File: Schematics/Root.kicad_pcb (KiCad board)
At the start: 2 copper layers, 100 x 100 mm, 138 parts, among them CON301 USB-MICRO-B, IC301 ATXMEGA256A3BU-A, J301 AVR_JTAG_Header, U1 LM324, U1001 PCA9685, U1101 PCA9685, U1201 PCA9685, U1301 PCA9685, U1401 PCA9685, U1501 PCA9685, U1601 PCA9685, U501 PCA9685, U601 PCA9685, U701 PCA9685, U801 PCA9685, U901 PCA9685

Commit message: LEDs are placed!
Worked out how to script KiCAD to do it too. Winner winner, time for a chicken dinner
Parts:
- removed C1001, C1101, C1201, C1301, C1401, C1501, C1601, C301, C302, C303, C304, C501, C601, C701, C801, C901: C, Capacitors_SMD:C_0603
- removed C201, C305, C311: 1u, Capacitors_SMD:C_0603
- removed C306, C307, C308, C309, C310: 100n, Capacitors_SMD:C_0603
- removed CON301: USB-MICRO-B, Connect:USB_Micro-B
- removed D1001, D1002, D1003, D1004, D1005, D1101, D1102, D1103, D1104, D1105, D1201, D1202, D1203, D1204, D1205, D1301, D1302, D1303, D1304, D1305, D1401, D1402, D1403, D1404, D1405, D1501, D1502, D1503, D1504, D1505, D1601, D1602, D1603, D1604, D1605, D501, D502, D503, D504, D505, D601, D602, D603, D604, D605, D701, D702, D703, D704, D705, D801, D802, D803, D804, D805, D901, D902, D903, D904, D905: LED_RGB, rgb:rgbled1
- removed IC301: ATXMEGA256A3BU-A, SMD_Packages:TQFP-64
- removed J301: AVR_JTAG_Header, Socket_Strips:Socket_Strip_Straight_2x05
- removed R1001, R1101, R1201, R1301, R1401, R1501, R1601, R501, R601, R701, R801, R901: 10k, Resistors_SMD:R_0603
- removed R301: 100R, Resistors_SMD:R_0603
- removed R302: 50R, Resistors_SMD:R_0603
- removed R303, R304: 47k, Resistors_SMD:R_0603
- removed U1001, U1101, U1201, U1301, U1401, U1501, U1601, U501, U601, U701, U801, U901: PCA9685, Housings_DFN_QFN:QFN-28-1EP_6x6mm_Pitch0.65mm
- added C10: C, Capacitors_SMD:C_0603, F.Cu at (248.8, 50.9)
- added C11: C, Capacitors_SMD:C_0603, F.Cu at (238.9, 59.1)
- added C12: C, Capacitors_SMD:C_0603, F.Cu at (257.7, 37.9)
- added C13: C, Capacitors_SMD:C_0603, F.Cu at (243.0, 52.6)
- added C14: 1u, Capacitors_SMD:C_0603, F.Cu at (234.0, 52.6)
- added C15: 100n, Capacitors_SMD:C_0603, F.Cu at (249.2, 44.4)
- added C16: 100n, Capacitors_SMD:C_0603, F.Cu at (238.5, 52.6)
- added C17: 100n, Capacitors_SMD:C_0603, F.Cu at (253.2, 37.9)
- added C18: 100n, Capacitors_SMD:C_0603, F.Cu at (234.4, 59.1)
- added C19: 100n, Capacitors_SMD:C_0603, F.Cu at (253.2, 50.9)
- added C20: 1u, Capacitors_SMD:C_0603, F.Cu at (248.8, 37.9)
- added C21: C, Capacitors_SMD:C_0603, F.Cu at (287.6, 49.6)
- added C22: C, Capacitors_SMD:C_0603, F.Cu at (238.4, 106.2)
- added C23: C, Capacitors_SMD:C_0603, F.Cu at (281.0, 80.9)
- added C24: C, Capacitors_SMD:C_0603, F.Cu at (333.5, 49.6)
- added C25: C, Capacitors_SMD:C_0603, F.Cu at (364.1, 99.4)
- added C26: C, Capacitors_SMD:C_0603, F.Cu at (280.2, 106.2)
- added C27: C, Capacitors_SMD:C_0603, F.Cu at (322.3, 74.5)
- added C28: C, Capacitors_SMD:C_0603, F.Cu at (363.0, 124.2)
- added C29: C, Capacitors_SMD:C_0603, F.Cu at (371.2, 49.6)
- added C30: C, Capacitors_SMD:C_0603, F.Cu at (318.7, 99.4)
- added C31: C, Capacitors_SMD:C_0603, F.Cu at (360.5, 74.5)
- added C32: C, Capacitors_SMD:C_0603, F.Cu at (322.0, 124.2)
- added C9: 100n, Capacitors_SMD:C_0603, F.Cu at (225.4, 82.1)
- added CON1: USB-MICRO-B, Connect:USB_Micro-B, F.Cu at (243.6, 40.5)
- added IC1: ATXMEGA256A3BU-A, SMD_Packages:TQFP-64, F.Cu at (105.5, 85.2)
- added J1: AVR_JTAG_Header, Socket_Strips:Socket_Strip_Straight_2x05, F.Cu at (225.0, 54.2)
- added LED1: LED_RGB, rgb:rgbled1, F.Cu at (100.6, 38.5)
- added LED10: LED_RGB, rgb:rgbled1, F.Cu at (64.8, 61.7)
- added LED11: LED_RGB, rgb:rgbled1, F.Cu at (62.6, 66.1)
- added LED12: LED_RGB, rgb:rgbled1, F.Cu at (60.8, 70.7)
- added LED13: LED_RGB, rgb:rgbled1, F.Cu at (59.5, 75.4)
- added LED14: LED_RGB, rgb:rgbled1, F.Cu at (58.8, 80.3)
- added LED15: LED_RGB, rgb:rgbled1, F.Cu at (58.5, 85.2)
- added LED16: LED_RGB, rgb:rgbled1, F.Cu at (58.8, 90.1)
- added LED17: LED_RGB, rgb:rgbled1, F.Cu at (59.5, 95.0)
- added LED18: LED_RGB, rgb:rgbled1, F.Cu at (60.8, 99.7)
- added LED19: LED_RGB, rgb:rgbled1, F.Cu at (62.6, 104.3)
- added LED2: LED_RGB, rgb:rgbled1, F.Cu at (95.7, 39.2)
- added LED20: LED_RGB, rgb:rgbled1, F.Cu at (64.8, 108.7)
- added LED21: LED_RGB, rgb:rgbled1, F.Cu at (67.5, 112.8)
- added LED22: LED_RGB, rgb:rgbled1, F.Cu at (70.6, 116.6)
- added LED23: LED_RGB, rgb:rgbled1, F.Cu at (74.1, 120.1)
- added LED24: LED_RGB, rgb:rgbled1, F.Cu at (77.9, 123.2)
- added LED25: LED_RGB, rgb:rgbled1, F.Cu at (82.0, 125.9)
- added LED26: LED_RGB, rgb:rgbled1, F.Cu at (86.4, 128.1)
- added LED27: LED_RGB, rgb:rgbled1, F.Cu at (91.0, 129.9)
- added LED28: LED_RGB, rgb:rgbled1, F.Cu at (95.7, 131.2)
- added LED29: LED_RGB, rgb:rgbled1, F.Cu at (100.6, 131.9)
- added LED3: LED_RGB, rgb:rgbled1, F.Cu at (91.0, 40.5)
- added LED30: LED_RGB, rgb:rgbled1, F.Cu at (105.5, 132.2)
- added LED31: LED_RGB, rgb:rgbled1, F.Cu at (110.4, 131.9)
- added LED32: LED_RGB, rgb:rgbled1, F.Cu at (115.3, 131.2)
- added LED33: LED_RGB, rgb:rgbled1, F.Cu at (120.0, 129.9)
- added LED34: LED_RGB, rgb:rgbled1, F.Cu at (124.6, 128.1)
- added LED35: LED_RGB, rgb:rgbled1, F.Cu at (129.0, 125.9)
- added LED36: LED_RGB, rgb:rgbled1, F.Cu at (133.1, 123.2)
- added LED37: LED_RGB, rgb:rgbled1, F.Cu at (136.9, 120.1)
- added LED38: LED_RGB, rgb:rgbled1, F.Cu at (140.4, 116.6)
- added LED39: LED_RGB, rgb:rgbled1, F.Cu at (143.5, 112.8)
- added LED4: LED_RGB, rgb:rgbled1, F.Cu at (86.4, 42.3)
- added LED40: LED_RGB, rgb:rgbled1, F.Cu at (146.2, 108.7)
- added LED41: LED_RGB, rgb:rgbled1, F.Cu at (148.4, 104.3)
- added LED42: LED_RGB, rgb:rgbled1, F.Cu at (150.2, 99.7)
- added LED43: LED_RGB, rgb:rgbled1, F.Cu at (151.5, 95.0)
- added LED44: LED_RGB, rgb:rgbled1, F.Cu at (152.2, 90.1)
- added LED45: LED_RGB, rgb:rgbled1, F.Cu at (152.5, 85.2)
- added LED46: LED_RGB, rgb:rgbled1, F.Cu at (152.2, 80.3)
- added LED47: LED_RGB, rgb:rgbled1, F.Cu at (151.5, 75.4)
- added LED48: LED_RGB, rgb:rgbled1, F.Cu at (150.2, 70.7)
- added LED49: LED_RGB, rgb:rgbled1, F.Cu at (148.4, 66.1)
- added LED5: LED_RGB, rgb:rgbled1, F.Cu at (82.0, 44.5)
- added LED50: LED_RGB, rgb:rgbled1, F.Cu at (146.2, 61.7)
- added LED51: LED_RGB, rgb:rgbled1, F.Cu at (143.5, 57.6)
- added LED52: LED_RGB, rgb:rgbled1, F.Cu at (140.4, 53.8)
- added LED53: LED_RGB, rgb:rgbled1, F.Cu at (136.9, 50.3)
- added LED54: LED_RGB, rgb:rgbled1, F.Cu at (133.1, 47.2)
- added LED55: LED_RGB, rgb:rgbled1, F.Cu at (129.0, 44.5)
- added LED56: LED_RGB, rgb:rgbled1, F.Cu at (124.6, 42.3)
- added LED57: LED_RGB, rgb:rgbled1, F.Cu at (120.0, 40.5)
- added LED58: LED_RGB, rgb:rgbled1, F.Cu at (115.3, 39.2)
- added LED59: LED_RGB, rgb:rgbled1, F.Cu at (110.4, 38.5)
- added LED6: LED_RGB, rgb:rgbled1, F.Cu at (77.9, 47.2)
- added LED60: LED_RGB, rgb:rgbled1, F.Cu at (105.5, 38.2)
- added LED7: LED_RGB, rgb:rgbled1, F.Cu at (74.1, 50.3)
- added LED8: LED_RGB, rgb:rgbled1, F.Cu at (70.6, 53.8)
- added LED9: LED_RGB, rgb:rgbled1, F.Cu at (67.5, 57.6)
- added R15: 100R, Resistors_SMD:R_0603, F.Cu at (254.2, 44.4)
- added R16: 50R, Resistors_SMD:R_0603, F.Cu at (258.7, 44.4)
- added R17: 47k, Resistors_SMD:R_0603, F.Cu at (261.8, 37.9)
- added R18: 47k, Resistors_SMD:R_0603, F.Cu at (243.0, 59.1)
- added R19: 10k, Resistors_SMD:R_0603, F.Cu at (291.7, 49.6)
- added R20: 10k, Resistors_SMD:R_0603, F.Cu at (234.4, 106.2)
- added R21: 10k, Resistors_SMD:R_0603, F.Cu at (276.9, 80.9)
- added R22: 10k, Resistors_SMD:R_0603, F.Cu at (329.4, 49.6)
- added R23: 10k, Resistors_SMD:R_0603, F.Cu at (360.1, 99.4)
- added R24: 10k, Resistors_SMD:R_0603, F.Cu at (276.2, 106.2)
- added R25: 10k, Resistors_SMD:R_0603, F.Cu at (318.3, 74.5)
- added R26: 10k, Resistors_SMD:R_0603, F.Cu at (358.9, 124.2)
- added R27: 10k, Resistors_SMD:R_0603, F.Cu at (375.3, 49.6)
- added R28: 10k, Resistors_SMD:R_0603, F.Cu at (322.8, 99.4)
- added R29: 10k, Resistors_SMD:R_0603, F.Cu at (364.6, 74.5)
- added R30: 10k, Resistors_SMD:R_0603, F.Cu at (318.0, 124.2)
- added U10: PCA9685, Housings_DFN_QFN:QFN-28-1EP_6x6mm_Pitch0.65mm, F.Cu at (345.8, 40.3)
- added U11: PCA9685, Housings_DFN_QFN:QFN-28-1EP_6x6mm_Pitch0.65mm, F.Cu at (335.1, 90.0)
- added U12: PCA9685, Housings_DFN_QFN:QFN-28-1EP_6x6mm_Pitch0.65mm, F.Cu at (334.4, 114.9)
- added U2: PCA9685, Housings_DFN_QFN:QFN-28-1EP_6x6mm_Pitch0.65mm, F.Cu at (334.7, 65.2)
- added U20: LM324, SMD_Packages:TSSOP-14, F.Cu at (221.0, 69.8)
- added U3: PCA9685, Housings_DFN_QFN:QFN-28-1EP_6x6mm_Pitch0.65mm, F.Cu at (304.0, 40.3)
- added U4: PCA9685, Housings_DFN_QFN:QFN-28-1EP_6x6mm_Pitch0.65mm, F.Cu at (293.3, 71.6)
- added U5: PCA9685, Housings_DFN_QFN:QFN-28-1EP_6x6mm_Pitch0.65mm, F.Cu at (387.6, 40.3)
- added U6: PCA9685, Housings_DFN_QFN:QFN-28-1EP_6x6mm_Pitch0.65mm, F.Cu at (376.9, 65.2)
- added U7: PCA9685, Housings_DFN_QFN:QFN-28-1EP_6x6mm_Pitch0.65mm, F.Cu at (292.6, 96.9)
- added U8: PCA9685, Housings_DFN_QFN:QFN-28-1EP_6x6mm_Pitch0.65mm, F.Cu at (374.5, 114.9)
- added U9: PCA9685, Housings_DFN_QFN:QFN-28-1EP_6x6mm_Pitch0.65mm, F.Cu at (250.8, 96.9)
- C7: value 100n -> 1u
- U1: value LM324 -> PCA9685; footprint SMD_Packages:TSSOP-14 -> Housings_DFN_QFN:QFN-28-1EP_6x6mm_Pitch0.65mm
- moved R4 134.1 mm to (252.1, 69.1)
- moved R7 133.4 mm to (247.8, 69.1), turned to 0 degrees
- moved R11 132.5 mm to (247.6, 82.0)
- moved R3 131.4 mm to (246.6, 75.6), turned to 0 degrees
- moved R2 128.6 mm to (250.5, 75.6), turned to 0 degrees
- moved R14 125.1 mm to (239.8, 69.1)
- moved R1 122.2 mm to (243.6, 82.1), turned to 0 degrees
- moved R10 121.1 mm to (243.8, 69.1), turned to 0 degrees
- moved R8 121.0 mm to (242.7, 75.6), turned to 0 degrees
- moved R9 119.1 mm to (238.8, 75.6), turned to 0 degrees
- moved R5 117.9 mm to (239.3, 82.1)
- moved C3 115.9 mm to (235.8, 69.1), turned to 0 degrees
- moved C8 115.7 mm to (230.4, 75.6), turned to 0 degrees
- moved R6 115.2 mm to (234.4, 82.1), turned to 0 degrees
- moved R12 113.1 mm to (234.9, 75.6), turned to 0 degrees
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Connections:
- C7 pad 1: Net-(C7-Pad1) -> GND
- C7 pad 2: Net-(C7-Pad2) -> VPP
- C8 pad 2: Net-(C7-Pad2) -> Net-(C8-Pad2)
- R10 pad 1: Net-(C7-Pad2) -> Net-(C8-Pad2)
- R11 pad 1: Net-(C8-Pad1) -> Net-(C9-Pad1)
- R11 pad 2: Net-(C7-Pad1) -> Net-(C8-Pad1)
- R14 pad 2: Net-(C8-Pad1) -> Net-(C9-Pad1)
- U1 pad 1: Net-(R7-Pad2) -> GND
- U1 pad 10: /Amp and Filter/V_com -> Net-(LED3-PadGC)
- U1 pad 12: /Amp and Filter/V_com -> Net-(LED3-PadBC)
- U1 pad 13: Net-(C7-Pad1) -> Net-(LED4-PadRC)
- U1 pad 14: Net-(C8-Pad1) -> Net-(LED4-PadGC)
- U1 pad 2: Net-(C2-Pad1) -> VPP
- U1 pad 3: /Amp and Filter/V_com -> Net-(LED1-PadRC)
- U1 pad 4: VPP -> Net-(LED1-PadGC)
- U1 pad 5: GND -> Net-(LED1-PadBC)
- U1 pad 6: Net-(R6-Pad1) -> Net-(LED2-PadRC)
- U1 pad 7: /Amp and Filter/AMP_OUT -> Net-(LED2-PadGC)
- U1 pad 8: Net-(C6-Pad1) -> Net-(LED2-PadBC)
- U1 pad 9: Net-(C5-Pad1) -> Net-(LED3-PadRC)

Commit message: Latest schematics and pcb.
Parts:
- added BT1: 3V, rgb:BU2032SM-HD-GTR-ND, F.Cu at (128.1, 85.1)
- added C1: C, Capacitors_SMD:C_1206, F.Cu at (92.8, 61.7)
- added JP1: JUMPER, SMD_Packages:SMD-0201_r, F.Cu at (99.1, 80.3)
- added R100: 100k, Resistors_SMD:R_0603, F.Cu at (97.7, 80.4)
- added X1: 12MHz, Crystals_Oscillators_SMD:crystal_FA238-TSX3225, F.Cu at (104.7, 76.6)
- added X2: 32.768KhZ, Crystals_Oscillators_SMD:crystal_FA238-TSX3225, F.Cu at (114.2, 84.1)
- CON1: footprint Connect:USB_Micro-B -> usb:USB_Micro-B; moved to B.Cu
- J1: footprint Socket_Strips:Socket_Strip_Straight_2x05 -> rgb:FTSH-105-01-L-DV-K-A-P
- R11: footprint Resistors_SMD:R_0402 -> Resistors_SMD:R_0603
- U20: footprint SMD_Packages:TSSOP-14 -> Housings_SOIC:SOIC-14_3.9x8.7mm_Pitch1.27mm
- moved U5 317.8 mm to (78.7, 114.9), turned to 318 degrees
- moved R27 298.9 mm to (83.1, 112.8)
- moved C29 296.5 mm to (81.1, 110.8)
- moved U6 285.9 mm to (97.2, 124.3), turned to 348 degrees
- moved C25 280.5 mm to (87.8, 51.0)
- moved R23 271.2 mm to (92.7, 54.0)
- moved C31 267.8 mm to (96.6, 119.8)
- moved R29 267.8 mm to (100.7, 119.8)
- moved U2 259.0 mm to (75.8, 58.4), turned to 228 degrees
- moved R25 242.3 mm to (76.2, 63.6)
- moved C27 241.3 mm to (81.6, 57.4)
- moved U3 240.4 mm to (66.4, 76.9), turned to 258 degrees
- moved U8 239.3 mm to (135.2, 112.0), turned to 48 degrees
- moved U12 231.0 mm to (113.8, 46.1), turned to 168 degrees
- moved C28 230.9 mm to (132.7, 107.2)
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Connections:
- IC1 pad 2: Net-(IC1-Pad2) -> (no net)
- IC1 pad 3: Net-(IC1-Pad3) -> (no net)
- IC1 pad 36: Net-(IC1-Pad36) -> (no net)
- IC1 pad 37: Net-(IC1-Pad37) -> (no net)
- IC1 pad 38: Net-(IC1-Pad38) -> (no net)
- IC1 pad 39: Net-(IC1-Pad39) -> (no net)
- IC1 pad 4: Net-(IC1-Pad4) -> (no net)
- IC1 pad 40: Net-(IC1-Pad40) -> (no net)
- IC1 pad 41: Net-(IC1-Pad41) -> (no net)
- IC1 pad 46: Net-(IC1-Pad46) -> (no net)
- IC1 pad 47: Net-(IC1-Pad47) -> (no net)
- IC1 pad 48: Net-(IC1-Pad48) -> (no net)
- IC1 pad 49: Net-(IC1-Pad49) -> (no net)
- IC1 pad 5: Net-(IC1-Pad5) -> /Microcontroller/RF_In
- IC1 pad 50: Net-(IC1-Pad50) -> (no net)
- IC1 pad 54: Net-(IC1-Pad54) -> (no net)
- IC1 pad 55: Net-(IC1-Pad55) -> (no net)
- IC1 pad 56: Net-(IC1-Pad56) -> (no net)
- IC1 pad 6: Net-(IC1-Pad6) -> (no net)
- IC1 pad 62: /Microcontroller/RF_In -> (no net)
- IC1 pad 63: Net-(IC1-Pad63) -> (no net)
- IC1 pad 64: Net-(IC1-Pad64) -> (no net)
- IC1 pad 7: Net-(IC1-Pad7) -> (no net)
- IC1 pad 8: Net-(IC1-Pad8) -> (no net)
- IC1 pad 9: Net-(IC1-Pad9) -> (no net)
- J1 pad 7: Net-(J1-Pad7) -> (no net)
- J1 pad 8: Net-(J1-Pad8) -> (no net)
- U1 pad 19: Net-(U1-Pad19) -> (no net)
- U10 pad 19: Net-(U10-Pad19) -> (no net)
- U11 pad 19: Net-(U11-Pad19) -> (no net)
- U12 pad 19: Net-(U12-Pad19) -> (no net)
- U2 pad 19: Net-(U2-Pad19) -> (no net)
- U3 pad 19: Net-(U3-Pad19) -> (no net)
- U4 pad 19: Net-(U4-Pad19) -> (no net)
- U5 pad 19: Net-(U5-Pad19) -> (no net)
- U6 pad 19: Net-(U6-Pad19) -> (no net)
- U7 pad 19: Net-(U7-Pad19) -> (no net)
- U8 pad 19: Net-(U8-Pad19) -> (no net)
- U9 pad 19: Net-(U9-Pad19) -> (no net)
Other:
- net class Clock removed
- net class Default: clearance 0.254 -> 0.15; trace_width 0.254 -> 0.15; via_dia 0.889 -> 0.3; via_drill 0.635 -> 0.25
- net class Power removed
- rule trace_clearance: 0.254 -> 0.15
- rule trace_min: 0.254 -> 0.15
- rule via_min_drill: 0.508 -> 0.25
- rule via_min_size: 0.889 -> 0.3

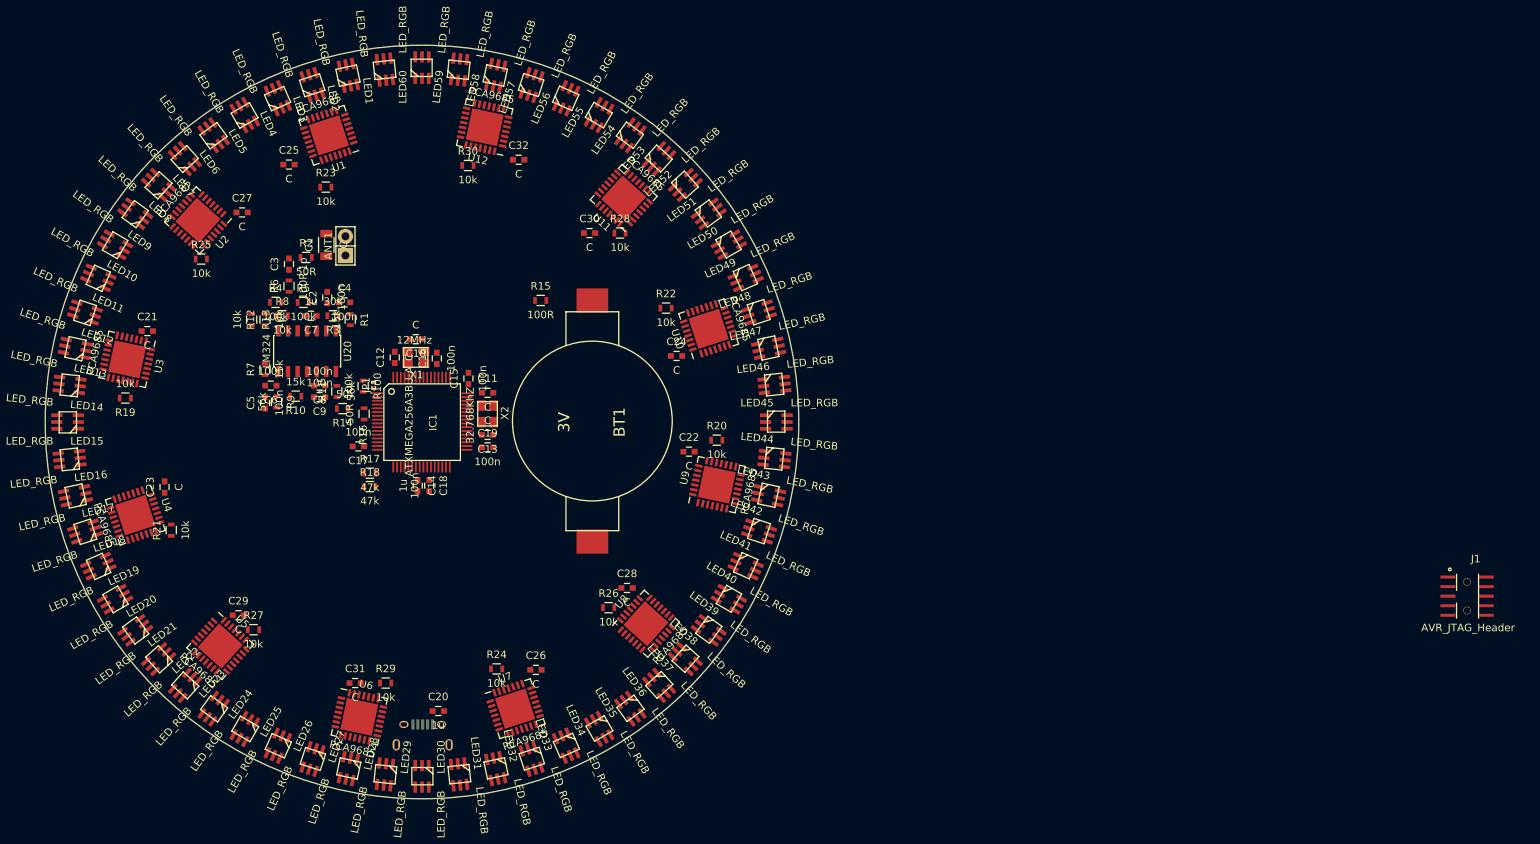
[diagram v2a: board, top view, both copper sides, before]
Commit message: Removed RF. Placed all LED drivers and passives and begun routing
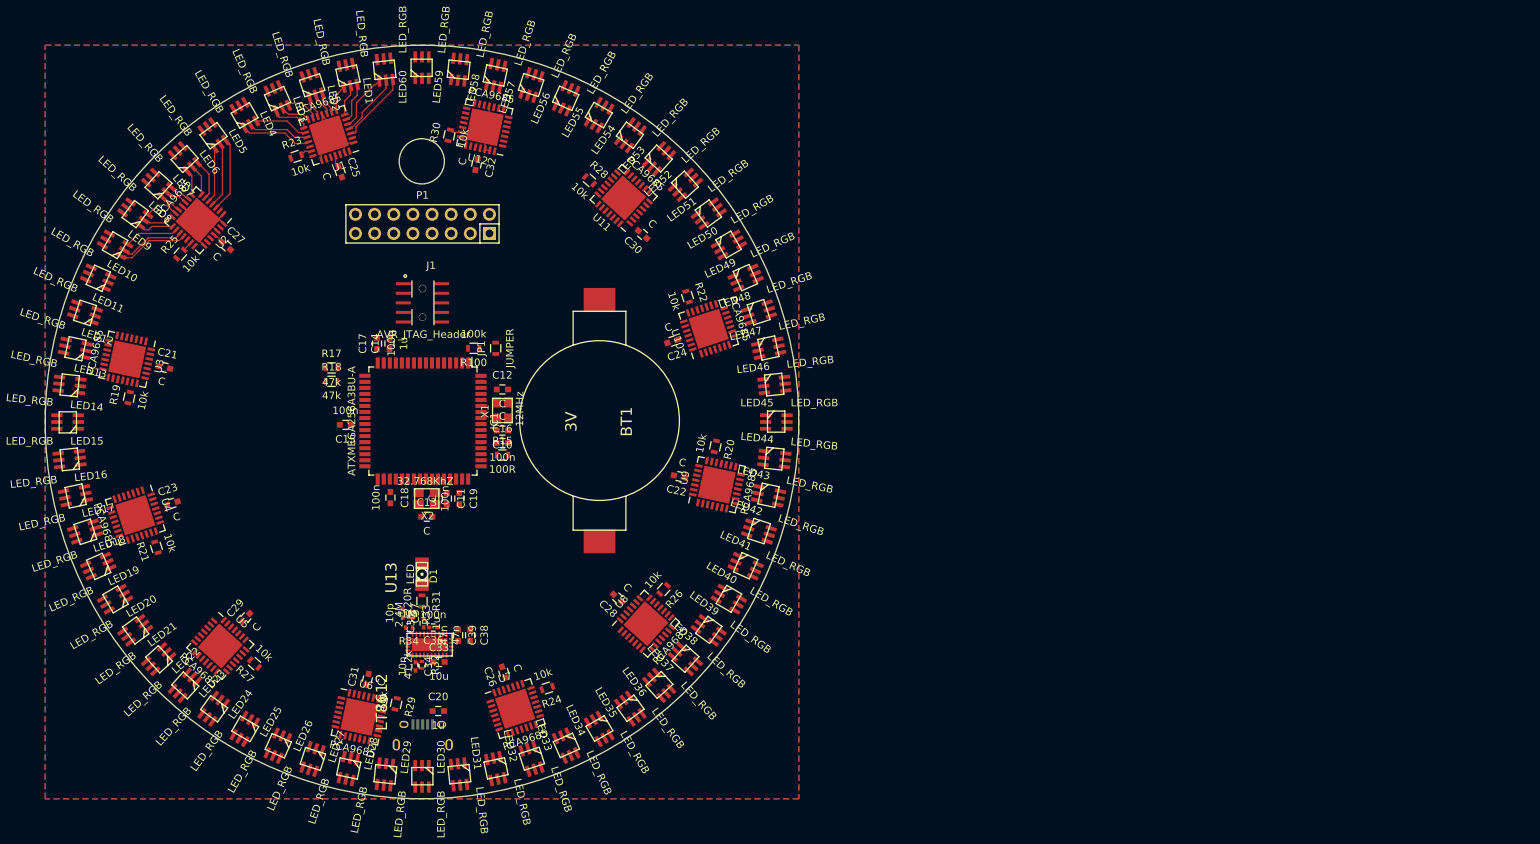
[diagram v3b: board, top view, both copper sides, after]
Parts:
- removed ANT1: ANT, Pin_Headers:Pin_Header_Straight_1x02
- removed C1: C, Capacitors_SMD:C_1206
- removed C2, C4, C5, C6, C8, C9: 100n, Capacitors_SMD:C_0603
- removed C3: 1p, Capacitors_SMD:C_0603
- removed C7: 1u, Capacitors_SMD:C_0603
- removed R1, R10, R7: 15k, Resistors_SMD:R_0603
- removed R11, R9: 56k, Resistors_SMD:R_0603
- removed R12, R13, R8: 10k, Resistors_SMD:R_0603
- removed R14: 50, Resistors_SMD:R_0603
- removed R16, R2: 50R, Resistors_SMD:R_0603
- removed R3: 30k, Resistors_SMD:R_0603
- removed R4, R5: 100k, Resistors_SMD:R_0603
- removed R6: 100R, Resistors_SMD:R_0603
- removed U20: LM324, Housings_SOIC:SOIC-14_3.9x8.7mm_Pitch1.27mm
- added C33: 10u, Capacitors_SMD:C_0603, F.Cu at (107.8, 117.0)
- added C34: 10n, Capacitors_SMD:C_0402, F.Cu at (104.6, 117.6)
- added C35: 1u, Capacitors_SMD:C_0402, F.Cu at (105.7, 111.9)
- added C36: 100n, Capacitors_SMD:C_0402, F.Cu at (107.0, 112.5)
- added C37: 10p, Capacitors_SMD:C_0402, F.Cu at (102.9, 110.6)
- added C38: 47n, Capacitors_SMD:C_0603, F.Cu at (111.9, 113.5)
- added C39: 47n, Capacitors_SMD:C_0603, F.Cu at (110.3, 113.5)
- added D1: LED, LEDs:LED-1206, F.Cu at (105.5, 105.4)
- added P1: CONN_02X08, Socket_Strips:Socket_Strip_Straight_2x08, F.Cu at (105.6, 58.9)
- added R31: 220R, Resistors_SMD:R_0603, F.Cu at (105.5, 108.9)
- added R32: 41.2k, Resistors_SMD:R_0402, F.Cu at (105.5, 117.4)
- added R33: 2.4M, Resistors_SMD:R_0402, F.Cu at (104.3, 110.8)
- added R34: 1M, Resistors_SMD:R_0402, F.Cu at (103.8, 112.5)
- added U13: LT8612, rgb:28QFN, F.Cu at (106.5, 114.8)
- IC1: footprint SMD_Packages:TQFP-64 -> Housings_QFP:TQFP-64_14x14mm_Pitch0.8mm
- JP1: footprint SMD_Packages:SMD-0201_r -> Resistors_SMD:R_0603
- moved J1 144.0 mm to (105.6, 69.4)
- moved R15 21.1 mm to (116.2, 89.6)
- moved C14 19.2 mm to (101.2, 74.8), turned to 90 degrees
- moved C15 17.4 mm to (95.3, 85.6), turned to 180 degrees
- moved JP1 16.9 mm to (115.3, 75.4)
- moved C10 16.7 mm to (116.2, 86.3)
- moved R100 15.5 mm to (112.4, 75.4), turned to 180 degrees
- moved C11 15.0 mm to (108.8, 95.4), turned to 270 degrees
- moved C12 14.9 mm to (116.2, 80.9), turned to 0 degrees
- moved R17 14.9 mm to (93.5, 78.0)
- moved R18 14.9 mm to (93.5, 79.8)
- moved C16 14.2 mm to (116.2, 88.0), turned to 0 degrees
- moved C17 13.9 mm to (99.5, 74.8), turned to 90 degrees
- moved X2 13.8 mm to (106.1, 95.4), turned to 180 degrees
- moved C13 13.5 mm to (106.1, 97.8), turned to 0 degrees
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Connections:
- net Net-(C20-Pad1) renamed /Power Supply/Vin
- IC1 pad 18: /Display/Display Sub block 1/~OE -> /Microcontroller/RX
- IC1 pad 19: /Display/Display Sub block 2/~OE -> /Microcontroller/TX
- IC1 pad 2: (no net) -> Net-(IC1-Pad2)
- IC1 pad 20: /Display/Display Sub block 3/~OE -> /Microcontroller/~CS
- IC1 pad 21: /Display/Display Sub block 4/~OE -> /Microcontroller/MOSI
- IC1 pad 22: /Display/Display Sub block 5/~OE -> /Microcontroller/MISO
- IC1 pad 23: /Display/Display Sub block 6/~OE -> /Microcontroller/SCK
- IC1 pad 3: (no net) -> Net-(IC1-Pad3)
- IC1 pad 36: (no net) -> /Display/Display Sub block 1/~OE
- IC1 pad 37: (no net) -> /Display/Display Sub block 2/~OE
- IC1 pad 38: (no net) -> /Display/Display Sub block 3/~OE
- IC1 pad 39: (no net) -> /Display/Display Sub block 4/~OE
- IC1 pad 4: (no net) -> Net-(IC1-Pad4)
- IC1 pad 40: (no net) -> /Display/Display Sub block 5/~OE
- IC1 pad 41: (no net) -> /Display/Display Sub block 6/~OE
- IC1 pad 46: (no net) -> Net-(IC1-Pad46)
- IC1 pad 47: (no net) -> Net-(IC1-Pad47)
- IC1 pad 48: (no net) -> Net-(IC1-Pad48)
- IC1 pad 49: (no net) -> Net-(IC1-Pad49)
- IC1 pad 5: /Microcontroller/RF_In -> Net-(IC1-Pad5)
- IC1 pad 50: (no net) -> Net-(IC1-Pad50)
- IC1 pad 54: (no net) -> Net-(IC1-Pad54)
- IC1 pad 55: (no net) -> Net-(IC1-Pad55)
- IC1 pad 56: (no net) -> Net-(IC1-Pad56)
- IC1 pad 6: (no net) -> Net-(IC1-Pad6)
- IC1 pad 62: (no net) -> Net-(IC1-Pad62)
- IC1 pad 63: (no net) -> Net-(IC1-Pad63)
- IC1 pad 64: (no net) -> Net-(IC1-Pad64)
- IC1 pad 7: (no net) -> Net-(IC1-Pad7)
- IC1 pad 8: (no net) -> Net-(IC1-Pad8)
- IC1 pad 9: (no net) -> Net-(IC1-Pad9)
- J1 pad 7: (no net) -> Net-(J1-Pad7)
- J1 pad 8: (no net) -> Net-(J1-Pad8)
- JP1 pad 1: Net-(IC1-Pad1) -> Net-(JP1-Pad1)
- R100 pad 2: Net-(IC1-Pad1) -> Net-(JP1-Pad1)
- U1 pad 19: (no net) -> Net-(U1-Pad19)
- U1 pad 22: (no net) -> GND
- U10 pad 19: (no net) -> Net-(U10-Pad19)
- U10 pad 22: (no net) -> GND
- U11 pad 19: (no net) -> Net-(U11-Pad19)
- U11 pad 22: (no net) -> GND
- U12 pad 19: (no net) -> Net-(U12-Pad19)
- U12 pad 22: (no net) -> GND
- U2 pad 19: (no net) -> Net-(U2-Pad19)
- U2 pad 22: (no net) -> GND
- U3 pad 19: (no net) -> Net-(U3-Pad19)
- U3 pad 22: (no net) -> GND
- U4 pad 19: (no net) -> Net-(U4-Pad19)
- U4 pad 22: (no net) -> GND
- U5 pad 19: (no net) -> Net-(U5-Pad19)
- U5 pad 22: (no net) -> GND
- U6 pad 19: (no net) -> Net-(U6-Pad19)
- U6 pad 22: (no net) -> GND
- U7 pad 19: (no net) -> Net-(U7-Pad19)
- U7 pad 22: (no net) -> GND
- U8 pad 19: (no net) -> Net-(U8-Pad19)
- U8 pad 22: (no net) -> GND
- U9 pad 19: (no net) -> Net-(U9-Pad19)
- U9 pad 22: (no net) -> GND
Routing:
- net GND: track 0.00 -> 32.5 mm
- net Net-(LED6-PadRC): track 0.00 -> 10.0 mm
- net Net-(LED1-PadRC): track 0.00 -> 9.75 mm
- net Net-(LED10-PadBC): track 0.00 -> 9.59 mm
- net Net-(LED5-PadBC): track 0.00 -> 9.46 mm
- net Net-(LED10-PadGC): track 0.00 -> 8.81 mm
- net Net-(LED6-PadGC): track 0.00 -> 8.70 mm
- net Net-(LED1-PadGC): track 0.00 -> 8.62 mm
- net Net-(LED5-PadGC): track 0.00 -> 8.24 mm
- net Net-(LED1-PadBC): track 0.00 -> 7.68 mm
- net Net-(LED6-PadBC): track 0.00 -> 7.36 mm
- net Net-(LED10-PadRC): track 0.00 -> 7.24 mm
- net Net-(LED5-PadRC): track 0.00 -> 7.19 mm
- net Net-(LED7-PadRC): track 0.00 -> 5.61 mm
- net Net-(LED2-PadRC): track 0.00 -> 5.37 mm
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- added copper zone on B.Cu, net GND
- added copper zone on F.Cu, net GND
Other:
- outline, holes or cut-outs redrawn
